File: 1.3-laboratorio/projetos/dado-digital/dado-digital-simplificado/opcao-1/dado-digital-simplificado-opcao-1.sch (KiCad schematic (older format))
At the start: 31 parts, among them J1 Conn_01x02, SW1 SW_DPST, SW2 SW_Push, U1 74HC74, U2 74HC74, U3 74HC14, U4 74HC08, U5 CD4511BE

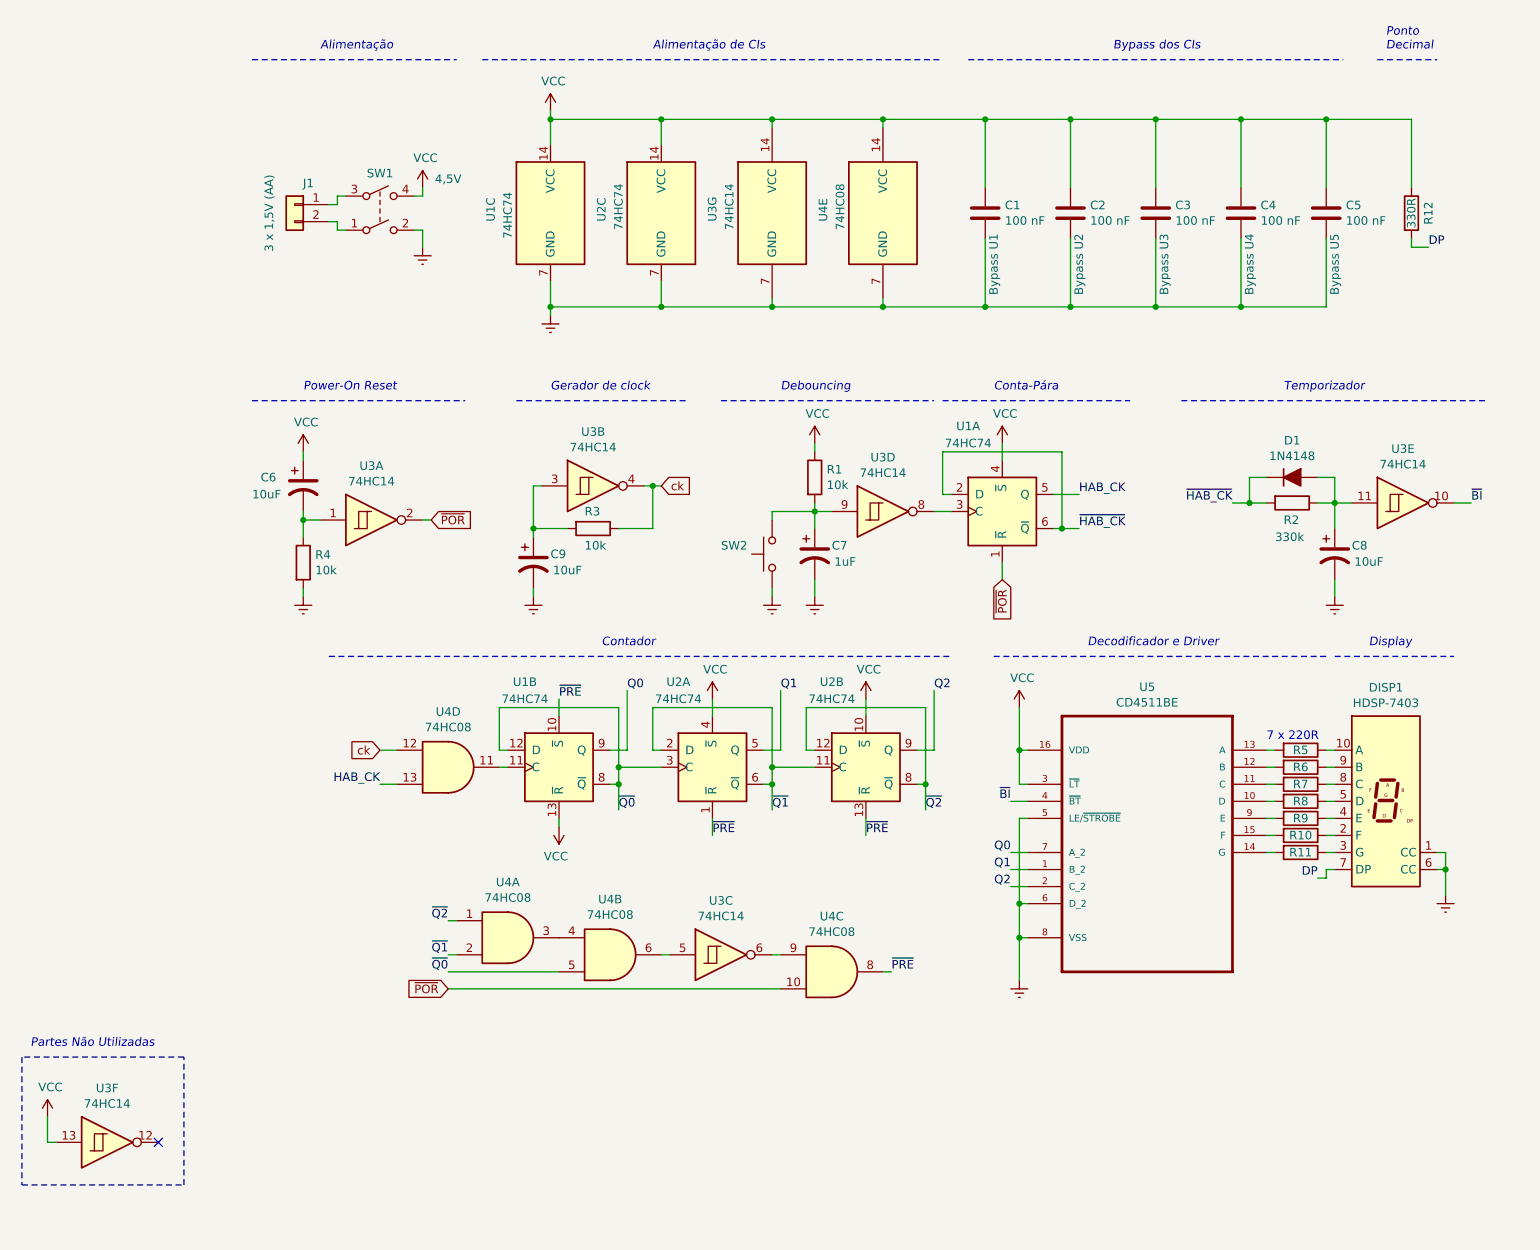
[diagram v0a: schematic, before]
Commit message: Revisões no projeto do Dado Digital Simplificado - Opção 1.
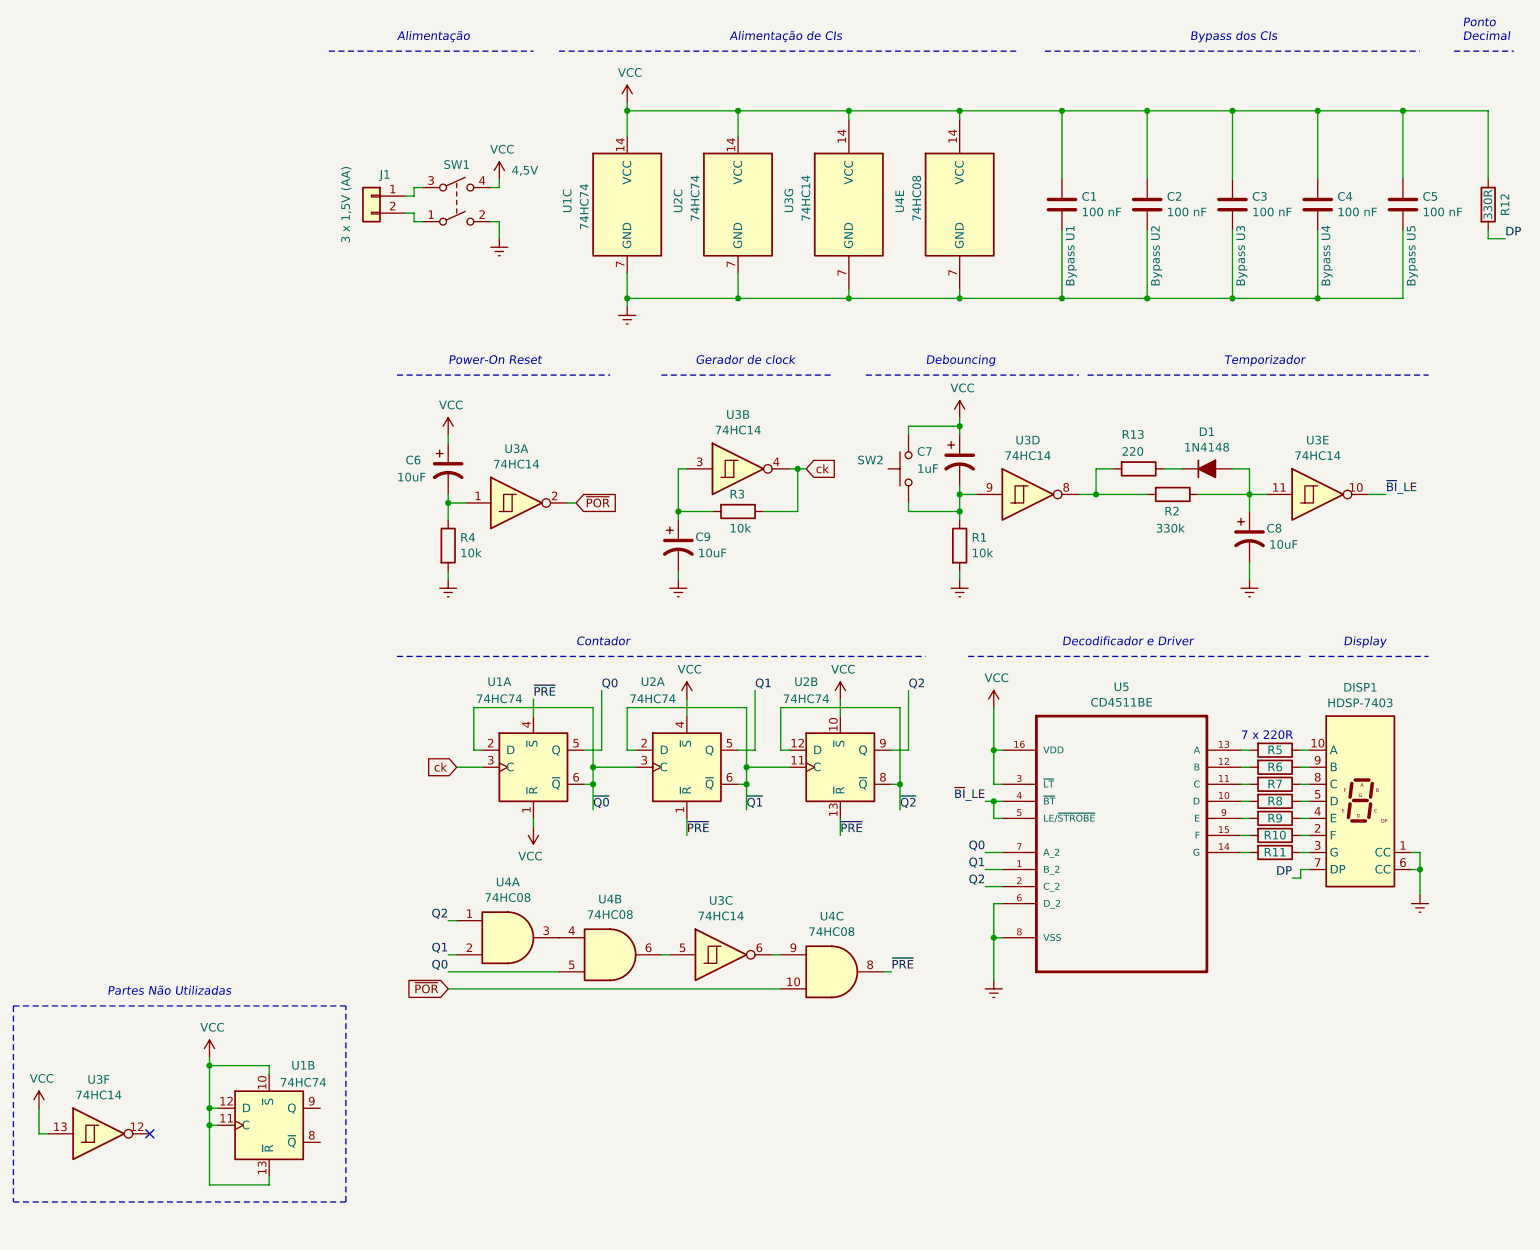
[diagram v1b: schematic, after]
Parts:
- removed unit 1 of U1
- removed unit 4 of U4
- added R13: 220, symbol Device:R
- added unit 2 of U1
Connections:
- net Earth: now also R1.2; no longer C7.2, SW2.1, U5.5 (LE/~STROBE)
- net Q0: now also U1.5 (Q), U4.5; no longer U1.9 (Q)
- net Q1: now also U4.2
- net Q2: now also U4.1
- net VCC: now also C7.1, SW2.2, U1.1 (~R), U1.10 (~S), U1.11 (C), U1.12 (D), U1.13 (~R); no longer R1.1, U1.13 (~R)
- net ck: now also U1.3 (C)
- net ~PRE: now also U1.4 (~S); no longer U1.10 (~S)
- net ~Q0: now also U1.2 (D), U1.6 (~Q); no longer U1.12 (D), U1.8 (~Q), U4.5
- net ~Q1: no longer U4.2
- net ~Q2: no longer U4.1
- net at U3.8: now also R2.2, R13.2
- net ~BI renamed ~BI~_LE
- net ~BI~_LE: now also U5.5 (LE/~STROBE)
- net ~HAB_CK: no longer names the net of D1.1 (K)
- net ~HAB_CK: now also R13.1; no longer R2.2
- new net: C7.2, R1.1, SW2.1, U3.9
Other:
- note removed: "Conta-Pára"
- moved on the sheet: C1, C2, C3, C4, C5, C6, C7, C8, C9, D1, DISP1, J1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

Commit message: Prova ETE102/Noturno P/2021.
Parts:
- C9: value 10uF -> 1uF
- R12: value 330R -> 220R
- R13: value 220 -> 220R
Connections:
- net DP: now also U1.9 (Q); no longer DISP1.7 (DP)
- net Q2: now also U1.11 (C)
- net VCC: no longer R12.1, U1.10 (~S), U1.11 (C), U1.12 (D), U3.13
- net ~BI~_LE: now also U3.13
- net at U3.12: now also U1.10 (~S)
- net at U1.8 (~Q): now also U1.12 (D)
- new net: DISP1.7 (DP), R12.1
- no-connect marks 1 -> 0
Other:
- note added: "(típico)"
- note added: "8 x 220R"
- note added: "Ponto Decimal"
- note added: "f ≅ 125Hz"
- note added: "Δt"
- note added: "Δt ≅ 116ms"
- note added: "Δt ≅ 2,5s"
- note removed: "7 x 220R"
- note removed: "Partes Não Utilizadas"
- note removed: "Ponto\nDecimal"
- moved on the sheet: DISP1, R10, R11, R12, R5, R6, R7, R8, R9, U1A, U1B, U2A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
